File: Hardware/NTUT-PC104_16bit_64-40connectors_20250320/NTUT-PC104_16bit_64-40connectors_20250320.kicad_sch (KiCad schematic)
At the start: 15 parts, among them J14 3V3, J15 5V0, J16 GND, J17 Conn_02x26_Odd_Even, J18 Conn_02x26_Odd_Even, J19 Conn_02x26_Odd_Even, J20 Conn_02x26_Odd_Even, J21 GND, J22 GND, J23 UNREG

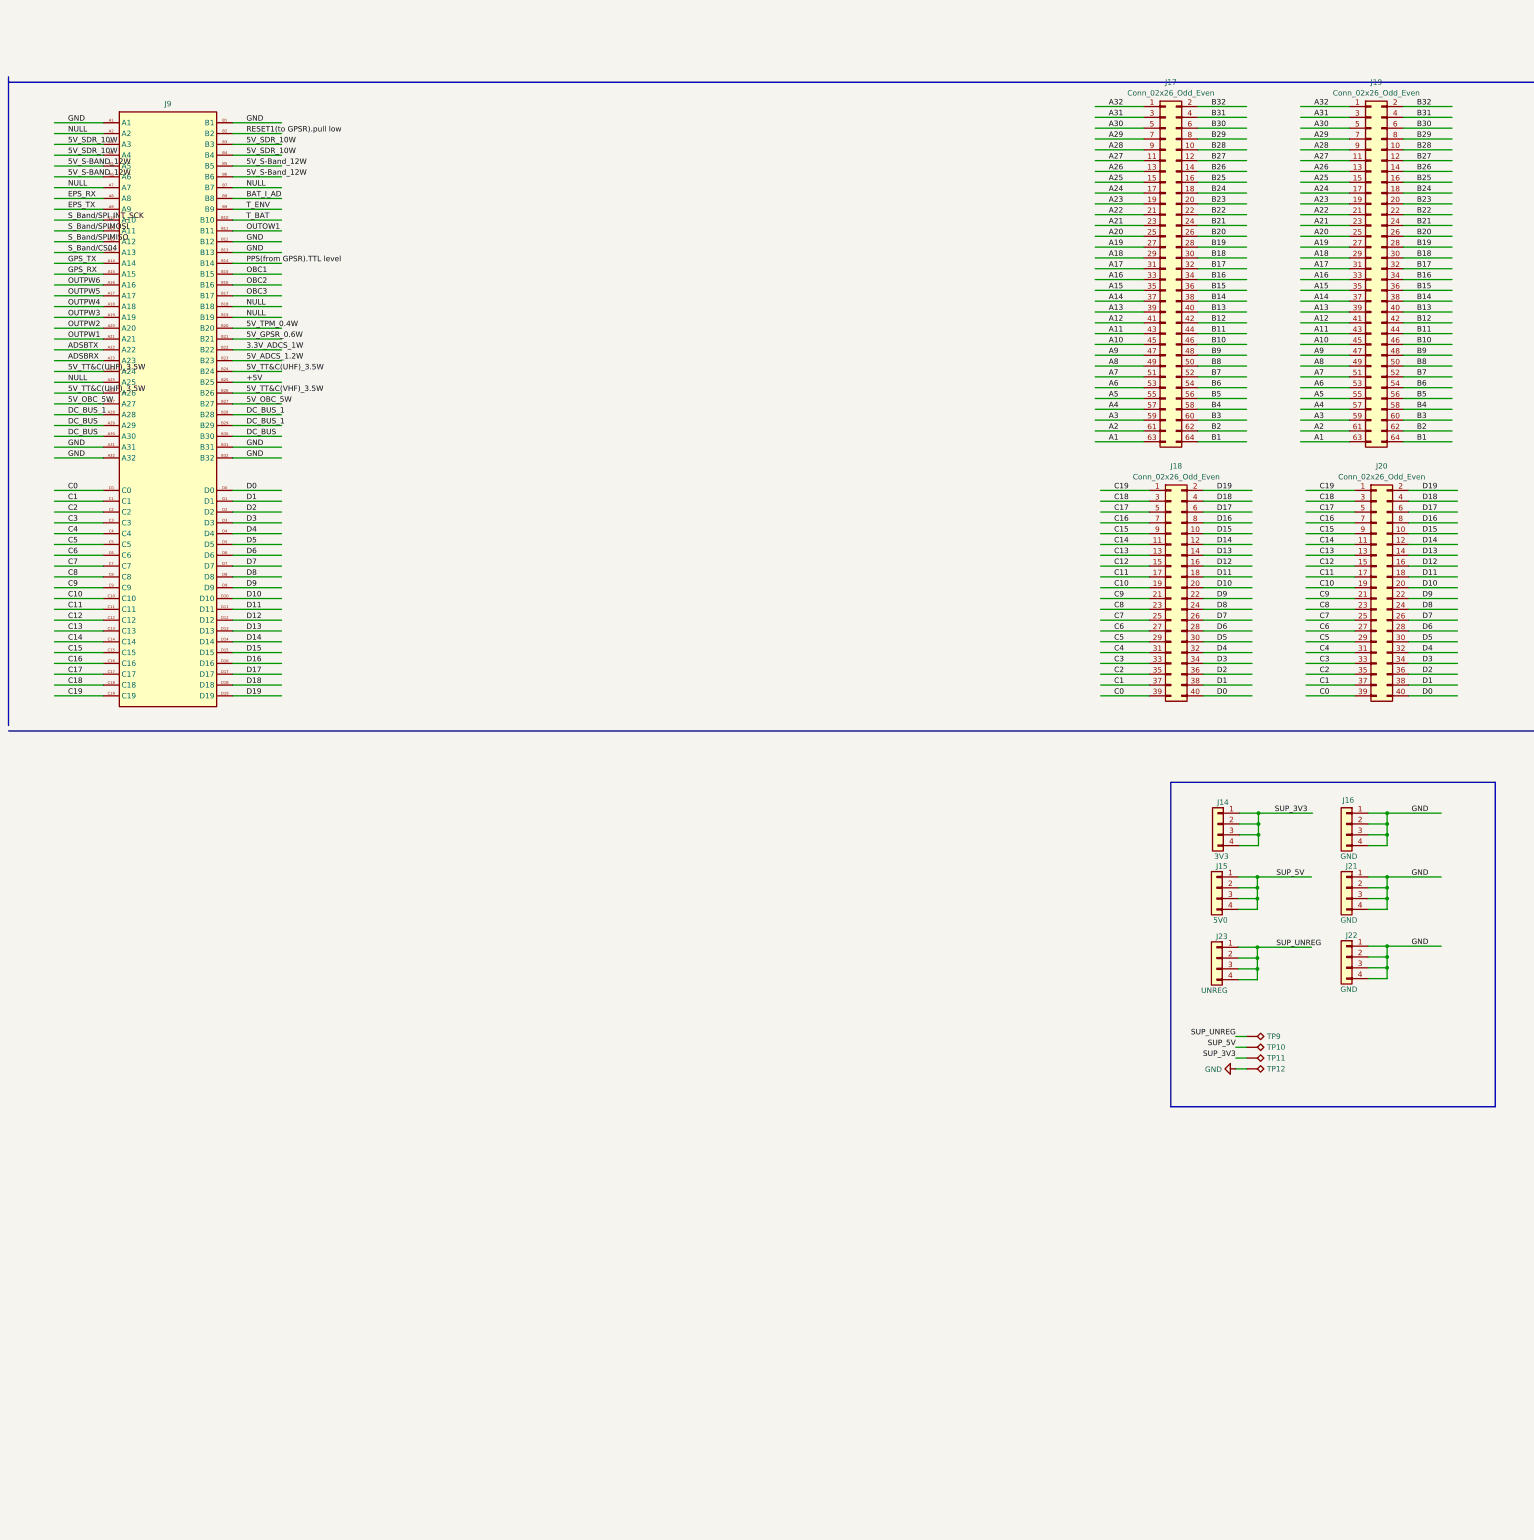
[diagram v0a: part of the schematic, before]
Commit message: Modify Schematic, assign GND to mount holes. Modify 64-pin and 40-pin labels.
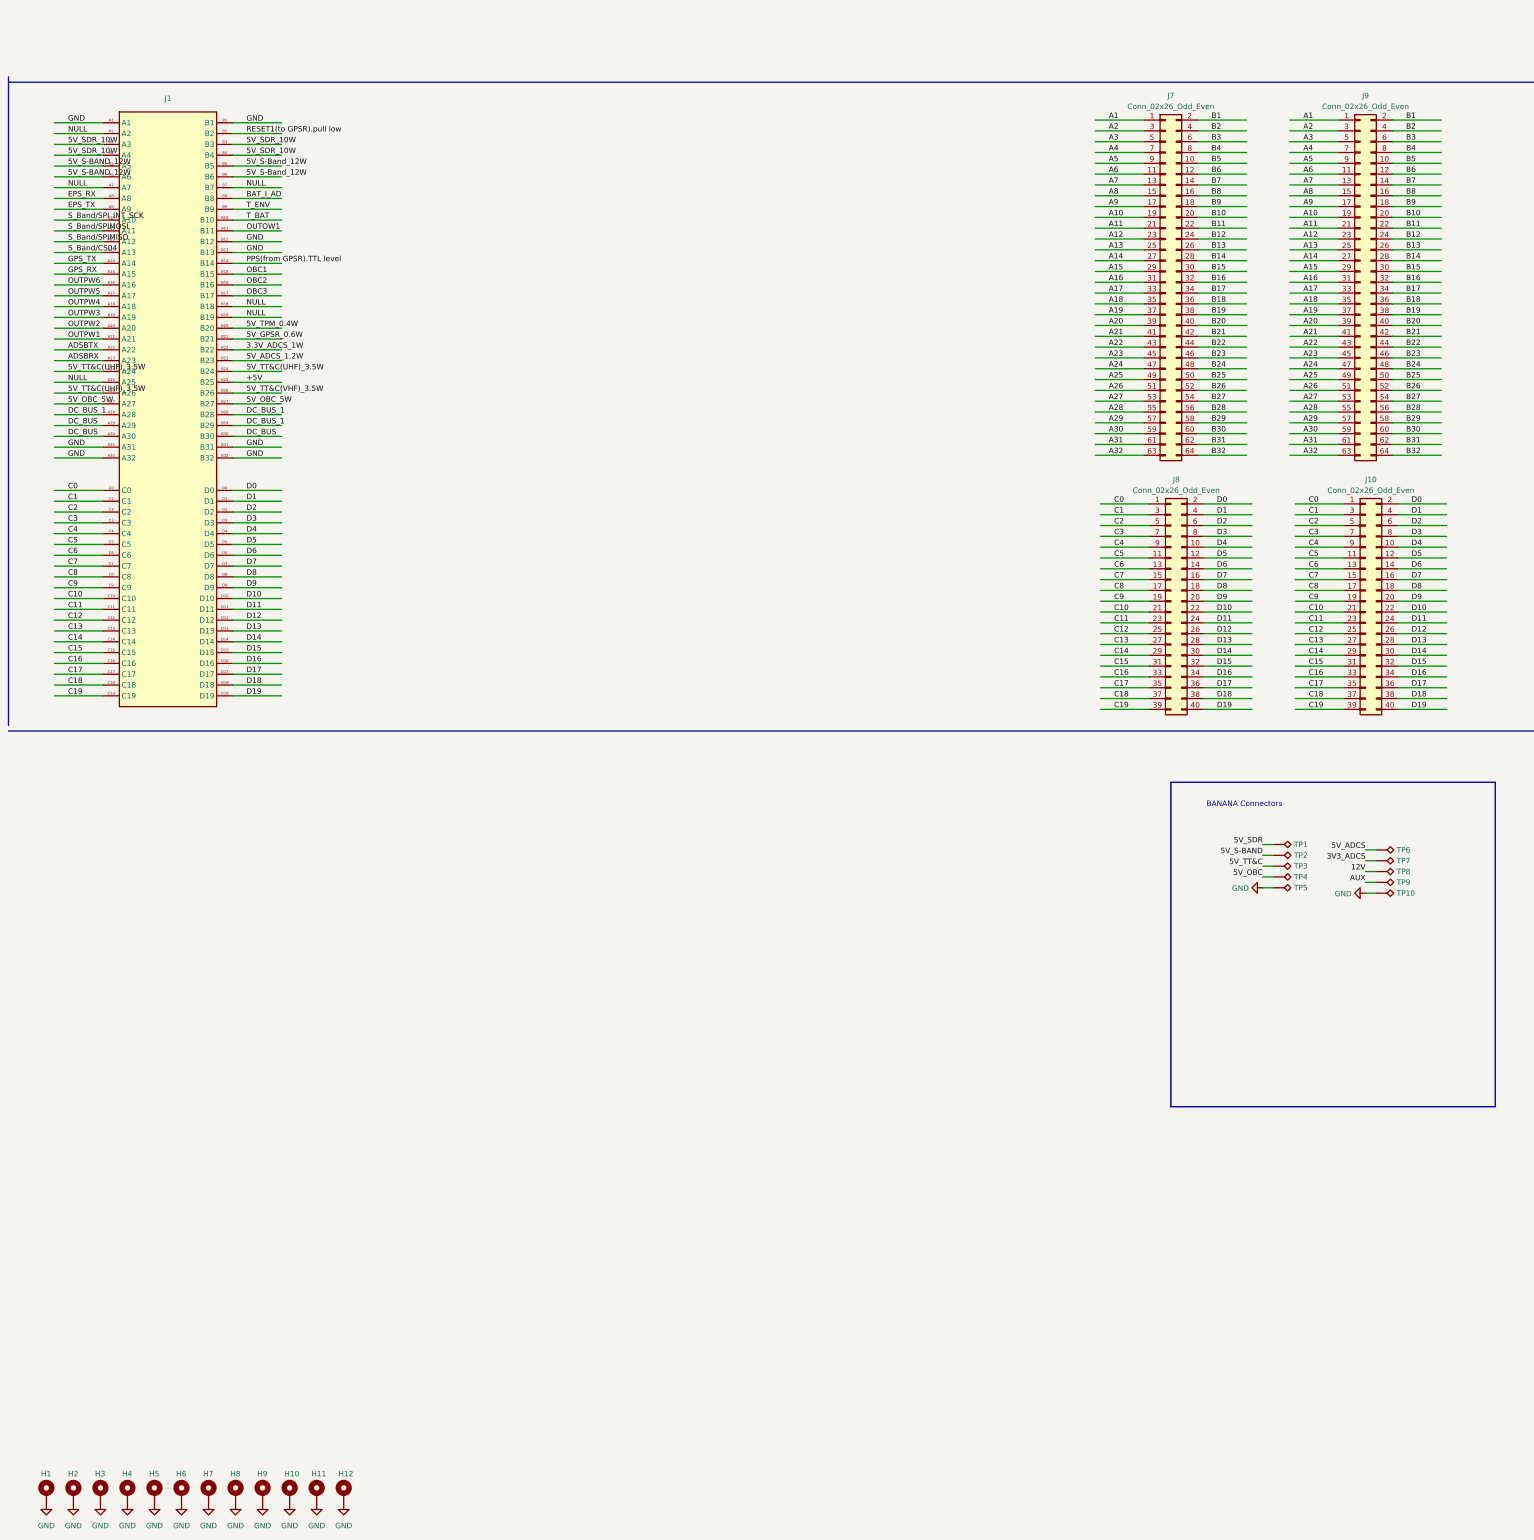
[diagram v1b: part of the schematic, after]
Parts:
- removed J14: 3V3, VST104_footprints:TSW-104-07-x-S, symbol Connector_Generic:Conn_01x04
- removed J15: 5V0, VST104_footprints:TSW-104-07-x-S, symbol Connector_Generic:Conn_01x04
- removed J16, J21, J22: GND, VST104_footprints:TSW-104-07-x-S, symbol Connector_Generic:Conn_01x04
- removed J19: Conn_02x26_Odd_Even, Connector_PinHeader_2.54mm:PinHeader_2x32_P2.54mm_Vertical, symbol Connector_Generic:Conn_02x32_Odd_Even
- removed J20: Conn_02x26_Odd_Even, Connector_PinHeader_2.54mm:PinHeader_2x20_P2.54mm_Vertical, symbol Connector_Generic:Conn_02x20_Odd_Even
- removed J23: UNREG, VST104_footprints:TSW-104-07-x-S, symbol Connector_Generic:Conn_01x04
- added H1, H10, H11, H12, H2, H3, H4, H5, H6, H7, H8, H9: MountingHole_Pad, VST104_footprints:MountingHole_3.2mm_M3_Pad_Via, symbol Mechanical:MountingHole_Pad
- added J10: Conn_02x26_Odd_Even, Connector_PinHeader_2.54mm:PinHeader_2x20_P2.54mm_Vertical, symbol Connector_Generic:Conn_02x20_Odd_Even
- added J9: Conn_02x26_Odd_Even, Connector_PinHeader_2.54mm:PinHeader_2x32_P2.54mm_Vertical, symbol Connector_Generic:Conn_02x32_Odd_Even
- added TP10, TP5, TP6, TP7, TP8, TP9: TestPoint_Alt, VST104_footprints:KSE_PN6095, symbol Connector:TestPoint_Alt
- renumbered J9 to J1, J17 to J7, J18 to J8, TP9 to TP1, TP10 to TP2, TP11 to TP3, TP12 to TP4
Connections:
- net A1: now also J7.1 (Pin_1), J9.1 (Pin_1); no longer J7.63 (Pin_63)
- net A10: now also J7.19 (Pin_19), J9.19 (Pin_19); no longer J7.45 (Pin_45)
- net A11: now also J7.21 (Pin_21), J9.21 (Pin_21); no longer J7.43 (Pin_43)
- net A12: now also J7.23 (Pin_23), J9.23 (Pin_23); no longer J7.41 (Pin_41)
- net A13: now also J7.25 (Pin_25), J9.25 (Pin_25); no longer J7.39 (Pin_39)
- net A14: now also J7.27 (Pin_27), J9.27 (Pin_27); no longer J7.37 (Pin_37)
- net A15: now also J7.29 (Pin_29), J9.29 (Pin_29); no longer J7.35 (Pin_35)
- net A16: now also J7.31 (Pin_31), J9.31 (Pin_31); no longer J7.33 (Pin_33)
- net A17: now also J7.33 (Pin_33), J9.33 (Pin_33); no longer J7.31 (Pin_31)
- net A18: now also J7.35 (Pin_35), J9.35 (Pin_35); no longer J7.29 (Pin_29)
- net A19: now also J7.37 (Pin_37), J9.37 (Pin_37); no longer J7.27 (Pin_27)
- net A2: now also J7.3 (Pin_3), J9.3 (Pin_3); no longer J7.61 (Pin_61)
- net A20: now also J7.39 (Pin_39), J9.39 (Pin_39); no longer J7.25 (Pin_25)
- net A21: now also J7.41 (Pin_41), J9.41 (Pin_41); no longer J7.23 (Pin_23)
- net A22: now also J7.43 (Pin_43), J9.43 (Pin_43); no longer J7.21 (Pin_21)
- net A23: now also J7.45 (Pin_45), J9.45 (Pin_45); no longer J7.19 (Pin_19)
- net A24: now also J7.47 (Pin_47), J9.47 (Pin_47); no longer J7.17 (Pin_17)
- net A25: now also J7.49 (Pin_49), J9.49 (Pin_49); no longer J7.15 (Pin_15)
- net A26: now also J7.51 (Pin_51), J9.51 (Pin_51); no longer J7.13 (Pin_13)
- net A27: now also J7.53 (Pin_53), J9.53 (Pin_53); no longer J7.11 (Pin_11)
- net A28: now also J7.55 (Pin_55), J9.55 (Pin_55); no longer J7.9 (Pin_9)
- net A29: now also J7.57 (Pin_57), J9.57 (Pin_57); no longer J7.7 (Pin_7)
- net A3: now also J7.5 (Pin_5), J9.5 (Pin_5); no longer J7.59 (Pin_59)
- net A30: now also J7.59 (Pin_59), J9.59 (Pin_59); no longer J7.5 (Pin_5)
- net A31: now also J7.61 (Pin_61), J9.61 (Pin_61); no longer J7.3 (Pin_3)
- net A32: now also J7.63 (Pin_63), J9.63 (Pin_63); no longer J7.1 (Pin_1)
- net A4: now also J7.7 (Pin_7), J9.7 (Pin_7); no longer J7.57 (Pin_57)
- net A5: now also J7.9 (Pin_9), J9.9 (Pin_9); no longer J7.55 (Pin_55)
- net A6: now also J7.11 (Pin_11), J9.11 (Pin_11); no longer J7.53 (Pin_53)
- net A7: now also J7.13 (Pin_13), J9.13 (Pin_13); no longer J7.51 (Pin_51)
- net A8: now also J7.15 (Pin_15), J9.15 (Pin_15); no longer J7.49 (Pin_49)
- net A9: now also J7.17 (Pin_17), J9.17 (Pin_17); no longer J7.47 (Pin_47)
- net B1: now also J7.2 (Pin_2), J9.2 (Pin_2); no longer J7.64 (Pin_64)
- net B10: now also J7.20 (Pin_20), J9.20 (Pin_20); no longer J7.46 (Pin_46)
- net B11: now also J7.22 (Pin_22), J9.22 (Pin_22); no longer J7.44 (Pin_44)
- net B12: now also J7.24 (Pin_24), J9.24 (Pin_24); no longer J7.42 (Pin_42)
- net B13: now also J7.26 (Pin_26), J9.26 (Pin_26); no longer J7.40 (Pin_40)
- net B14: now also J7.28 (Pin_28), J9.28 (Pin_28); no longer J7.38 (Pin_38)
- net B15: now also J7.30 (Pin_30), J9.30 (Pin_30); no longer J7.36 (Pin_36)
- net B16: now also J7.32 (Pin_32), J9.32 (Pin_32); no longer J7.34 (Pin_34)
- net B17: now also J7.34 (Pin_34), J9.34 (Pin_34); no longer J7.32 (Pin_32)
- net B18: now also J7.36 (Pin_36), J9.36 (Pin_36); no longer J7.30 (Pin_30)
- net B19: now also J7.38 (Pin_38), J9.38 (Pin_38); no longer J7.28 (Pin_28)
- net B2: now also J7.4 (Pin_4), J9.4 (Pin_4); no longer J7.62 (Pin_62)
- net B20: now also J7.40 (Pin_40), J9.40 (Pin_40); no longer J7.26 (Pin_26)
- net B21: now also J7.42 (Pin_42), J9.42 (Pin_42); no longer J7.24 (Pin_24)
- net B22: now also J7.44 (Pin_44), J9.44 (Pin_44); no longer J7.22 (Pin_22)
- net B23: now also J7.46 (Pin_46), J9.46 (Pin_46); no longer J7.20 (Pin_20)
- net B24: now also J7.48 (Pin_48), J9.48 (Pin_48); no longer J7.18 (Pin_18)
- net B25: now also J7.50 (Pin_50), J9.50 (Pin_50); no longer J7.16 (Pin_16)
- net B26: now also J7.52 (Pin_52), J9.52 (Pin_52); no longer J7.14 (Pin_14)
- net B27: now also J7.54 (Pin_54), J9.54 (Pin_54); no longer J7.12 (Pin_12)
- net B28: now also J7.56 (Pin_56), J9.56 (Pin_56); no longer J7.10 (Pin_10)
- net B29: now also J7.58 (Pin_58), J9.58 (Pin_58); no longer J7.8 (Pin_8)
- net B3: now also J7.6 (Pin_6), J9.6 (Pin_6); no longer J7.60 (Pin_60)
- net B30: now also J7.60 (Pin_60), J9.60 (Pin_60); no longer J7.6 (Pin_6)
- net B31: now also J7.62 (Pin_62), J9.62 (Pin_62); no longer J7.4 (Pin_4)
- net B32: now also J7.64 (Pin_64), J9.64 (Pin_64); no longer J7.2 (Pin_2)
- net B4: now also J7.8 (Pin_8), J9.8 (Pin_8); no longer J7.58 (Pin_58)
- net B5: now also J7.10 (Pin_10), J9.10 (Pin_10); no longer J7.56 (Pin_56)
- net B6: now also J7.12 (Pin_12), J9.12 (Pin_12); no longer J7.54 (Pin_54)
- net B7: now also J7.14 (Pin_14), J9.14 (Pin_14); no longer J7.52 (Pin_52)
- net B8: now also J7.16 (Pin_16), J9.16 (Pin_16); no longer J7.50 (Pin_50)
- net B9: now also J7.18 (Pin_18), J9.18 (Pin_18); no longer J7.48 (Pin_48)
- net C0: now also J8.1 (Pin_1), J10.1 (Pin_1); no longer J8.39 (Pin_39)
- net C1: now also J8.3 (Pin_3), J10.3 (Pin_3); no longer J8.37 (Pin_37)
- net C10: now also J8.21 (Pin_21), J10.21 (Pin_21); no longer J8.19 (Pin_19)
- net C11: now also J8.23 (Pin_23), J10.23 (Pin_23); no longer J8.17 (Pin_17)
- net C12: now also J8.25 (Pin_25), J10.25 (Pin_25); no longer J8.15 (Pin_15)
- net C13: now also J8.27 (Pin_27), J10.27 (Pin_27); no longer J8.13 (Pin_13)
- net C14: now also J8.29 (Pin_29), J10.29 (Pin_29); no longer J8.11 (Pin_11)
- net C15: now also J8.31 (Pin_31), J10.31 (Pin_31); no longer J8.9 (Pin_9)
- net C16: now also J8.33 (Pin_33), J10.33 (Pin_33); no longer J8.7 (Pin_7)
- net C17: now also J8.35 (Pin_35), J10.35 (Pin_35); no longer J8.5 (Pin_5)
- net C18: now also J8.37 (Pin_37), J10.37 (Pin_37); no longer J8.3 (Pin_3)
- net C19: now also J8.39 (Pin_39), J10.39 (Pin_39); no longer J8.1 (Pin_1)
- net C2: now also J8.5 (Pin_5), J10.5 (Pin_5); no longer J8.35 (Pin_35)
- net C3: now also J8.7 (Pin_7), J10.7 (Pin_7); no longer J8.33 (Pin_33)
- net C4: now also J8.9 (Pin_9), J10.9 (Pin_9); no longer J8.31 (Pin_31)
- net C5: now also J8.11 (Pin_11), J10.11 (Pin_11); no longer J8.29 (Pin_29)
- net C6: now also J8.13 (Pin_13), J10.13 (Pin_13); no longer J8.27 (Pin_27)
- net C7: now also J8.15 (Pin_15), J10.15 (Pin_15); no longer J8.25 (Pin_25)
- net C8: now also J8.17 (Pin_17), J10.17 (Pin_17); no longer J8.23 (Pin_23)
- net C9: now also J8.19 (Pin_19), J10.19 (Pin_19); no longer J8.21 (Pin_21)
- net D0: now also J8.2 (Pin_2), J10.2 (Pin_2); no longer J8.40 (Pin_40)
- net D1: now also J8.4 (Pin_4), J10.4 (Pin_4); no longer J8.38 (Pin_38)
- net D10: now also J8.22 (Pin_22), J10.22 (Pin_22); no longer J8.20 (Pin_20)
- net D11: now also J8.24 (Pin_24), J10.24 (Pin_24); no longer J8.18 (Pin_18)
- net D12: now also J8.26 (Pin_26), J10.26 (Pin_26); no longer J8.16 (Pin_16)
- net D13: now also J8.28 (Pin_28), J10.28 (Pin_28); no longer J8.14 (Pin_14)
- net D14: now also J8.30 (Pin_30), J10.30 (Pin_30); no longer J8.12 (Pin_12)
- net D15: now also J8.32 (Pin_32), J10.32 (Pin_32); no longer J8.10 (Pin_10)
- net D16: now also J8.34 (Pin_34), J10.34 (Pin_34); no longer J8.8 (Pin_8)
- net D17: now also J8.36 (Pin_36), J10.36 (Pin_36); no longer J8.6 (Pin_6)
- net D18: now also J8.38 (Pin_38), J10.38 (Pin_38); no longer J8.4 (Pin_4)
- net D19: now also J8.40 (Pin_40), J10.40 (Pin_40); no longer J8.2 (Pin_2)
- net D2: now also J8.6 (Pin_6), J10.6 (Pin_6); no longer J8.36 (Pin_36)
- net D3: now also J8.8 (Pin_8), J10.8 (Pin_8); no longer J8.34 (Pin_34)
- net D4: now also J8.10 (Pin_10), J10.10 (Pin_10); no longer J8.32 (Pin_32)
- net D5: now also J8.12 (Pin_12), J10.12 (Pin_12); no longer J8.30 (Pin_30)
- net D6: now also J8.14 (Pin_14), J10.14 (Pin_14); no longer J8.28 (Pin_28)
- net D7: now also J8.16 (Pin_16), J10.16 (Pin_16); no longer J8.26 (Pin_26)
- net D8: now also J8.18 (Pin_18), J10.18 (Pin_18); no longer J8.24 (Pin_24)
- net D9: now also J8.20 (Pin_20), J10.20 (Pin_20); no longer J8.22 (Pin_22)
- net GND: now also H1.1, H10.1, H11.1, H12.1, H2.1, H3.1, H4.1, H5.1, H6.1, H7.1, H8.1, H9.1, TP10.1, TP5.1; no longer TP4.1
- net SUP_3V3 renamed 5V_TT&C
- net SUP_5V renamed 5V_S-BAND
- net SUP_UNREG renamed 5V_SDR
- new net 12V: TP8.1
- new net 3V3_ADCS: TP7.1
- new net 5V_ADCS: TP6.1
- new net 5V_OBC: TP4.1
- new net AUX: TP9.1
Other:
- note added: "BANANA Connectors"
- moved on the sheet: J7, J8, TP1, TP2, TP3, TP4

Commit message: 1. Add all six boards. 2. Assign Parus pins to every board. 3. Change foot-print path to project directory such that the project    will not rely on external footprints. 4. Copy 'CubeSat_PC104_16bit_footprint.kicad_mod',    'CubeSat_PC104_16bit_footprint_15mm.kicad_mod' and    'CubeSat_PC104_16bit_footprint_Edge.Cut.kicad_mod' to project footprint    directory. 5. Add connectors between banana connectors and all other boards.
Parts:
- added J11: ~, VST104_footprints:PC104_16bit_Connector, symbol VST104_symbols:PC104
- added J12, J13, J14, J15, J16, J17, J18, J7: Conn_02x04_Odd_Even, Connector_PinHeader_2.54mm:PinHeader_2x04_P2.54mm_Vertical, symbol Connector_Generic:Conn_02x04_Odd_Even
- added J2, J3, J4, J5, J6: ~, VST104_footprints:CubeSat_PC104_16bit_footprint, symbol VST104_symbols:PC104
- renumbered J7 to JA19
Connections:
- net A1 is gone; now on net GND: J9.1 (Pin_1), JA19.1 (Pin_1)
- net A10 is gone; now on net S_Band/SPI_INT_SCK: J9.19 (Pin_19), JA19.19 (Pin_19)
- net A11 is gone; now on net S_Band/SPIMOSI: J9.21 (Pin_21), JA19.21 (Pin_21)
- net A12 is gone; now on net S_Band/SPIMISO: J9.23 (Pin_23), JA19.23 (Pin_23)
- net A13 is gone; now on net S_Band/CS04: J9.25 (Pin_25), JA19.25 (Pin_25)
- net A14 is gone; now on net GPS_TX: J9.27 (Pin_27), JA19.27 (Pin_27)
- net A15 is gone; now on net GPS_RX: J9.29 (Pin_29), JA19.29 (Pin_29)
- net A16 is gone; now on net OUTPW6: J9.31 (Pin_31), JA19.31 (Pin_31)
- net A17 is gone; now on net OUTPW5: J9.33 (Pin_33), JA19.33 (Pin_33)
- net A18 is gone; now on net OUTPW4: J9.35 (Pin_35), JA19.35 (Pin_35)
- net A19 is gone; now on net OUTPW3: J9.37 (Pin_37), JA19.37 (Pin_37)
- net A20 is gone; now on net OUTPW2: J9.39 (Pin_39), JA19.39 (Pin_39)
- net A21 is gone; now on net OUTPW1: J9.41 (Pin_41), JA19.41 (Pin_41)
- net A22 is gone; now on net ADSBTX: J9.43 (Pin_43), JA19.43 (Pin_43)
- net A23 is gone; now on net ADSBRX: J9.45 (Pin_45), JA19.45 (Pin_45)
- net A24 is gone; now on net 5V_TT&C(UHF)_3.5W: J9.47 (Pin_47), JA19.47 (Pin_47)
- net A26 is gone; now on net 5V_TT&C(VHF)_3.5W: J9.51 (Pin_51), JA19.51 (Pin_51)
- net A27 is gone; now on net 5V_OBC_5W: J9.53 (Pin_53), JA19.53 (Pin_53)
- net A28 is gone; now on net DC_BUS_1: J9.55 (Pin_55), JA19.55 (Pin_55)
- net A29 is gone; now on net DC_BUS: J9.57 (Pin_57), JA19.57 (Pin_57)
- net A3 is gone; now on net 5V_SDR_10W: J9.5 (Pin_5), JA19.5 (Pin_5)
- net A30 is gone; now on net DC_BUS: J9.59 (Pin_59), JA19.59 (Pin_59)
- net A31 is gone; now on net GND: J9.61 (Pin_61), JA19.61 (Pin_61)
- net A32 is gone; now on net GND: J9.63 (Pin_63), JA19.63 (Pin_63)
- net A4 is gone; now on net 5V_SDR_10W: J9.7 (Pin_7), JA19.7 (Pin_7)
- net A5 is gone; now on net 5V_S-BAND_12W: J9.9 (Pin_9), JA19.9 (Pin_9)
- net A6 is gone; now on net 5V_S-BAND_12W: J9.11 (Pin_11), JA19.11 (Pin_11)
- net A8 is gone; now on net EPS_RX: J9.15 (Pin_15), JA19.15 (Pin_15)
- net A9 is gone; now on net EPS_TX: J9.17 (Pin_17), JA19.17 (Pin_17)
- net B1 is gone; now on net GND: J9.2 (Pin_2), JA19.2 (Pin_2)
- net B10 is gone; now on net T_BAT: J9.20 (Pin_20), JA19.20 (Pin_20)
- net B11 is gone; now on net OUTOW1: J9.22 (Pin_22), JA19.22 (Pin_22)
- net B12 is gone; now on net GND: J9.24 (Pin_24), JA19.24 (Pin_24)
- net B13 is gone; now on net GND: J9.26 (Pin_26), JA19.26 (Pin_26)
- net B15 is gone; now on net OBC1: J9.30 (Pin_30), JA19.30 (Pin_30)
- net B16 is gone; now on net OBC2: J9.32 (Pin_32), JA19.32 (Pin_32)
- net B17 is gone; now on net OBC3: J9.34 (Pin_34), JA19.34 (Pin_34)
- net B20 is gone; now on net 5V_TPM_0.4W: J9.40 (Pin_40), JA19.40 (Pin_40)
- net B21 is gone; now on net 5V_GPSR_0.6W: J9.42 (Pin_42), JA19.42 (Pin_42)
- net B22 is gone; now on net 3.3V_ADCS_1W: J9.44 (Pin_44), JA19.44 (Pin_44)
- net B23 is gone; now on net 5V_ADCS_1.2W: J9.46 (Pin_46), JA19.46 (Pin_46)
- net B24 is gone; now on net 5V_TT&C(UHF)_3.5W: J9.48 (Pin_48), JA19.48 (Pin_48)
- net B25 is gone; now on net +5V: J9.50 (Pin_50), JA19.50 (Pin_50)
- net B26 is gone; now on net 5V_TT&C(VHF)_3.5W: J9.52 (Pin_52), JA19.52 (Pin_52)
- net B27 is gone; now on net 5V_OBC_5W: J9.54 (Pin_54), JA19.54 (Pin_54)
- net B28 is gone; now on net DC_BUS_1: J9.56 (Pin_56), JA19.56 (Pin_56)
- net B29 is gone; now on net DC_BUS_1: J9.58 (Pin_58), JA19.58 (Pin_58)
- net B3 is gone; now on net 5V_SDR_10W: J9.6 (Pin_6), JA19.6 (Pin_6)
- net B30 is gone; now on net DC_BUS: J9.60 (Pin_60), JA19.60 (Pin_60)
- net B31 is gone; now on net GND: J9.62 (Pin_62), JA19.62 (Pin_62)
- net B32 is gone; now on net GND: J9.64 (Pin_64), JA19.64 (Pin_64)
- net B4 is gone; now on net 5V_SDR_10W: J9.8 (Pin_8), JA19.8 (Pin_8)
- net B5 is gone; now on net 5V_S-Band_12W: J9.10 (Pin_10), JA19.10 (Pin_10)
- net B6 is gone; now on net 5V_S-Band_12W: J9.12 (Pin_12), JA19.12 (Pin_12)
- net B8 is gone; now on net BAT_I_AD: J9.16 (Pin_16), JA19.16 (Pin_16)
- net B9 is gone; now on net T_ENV: J9.18 (Pin_18), JA19.18 (Pin_18)
- net PPS(from GPSR).TTL level is gone; now on net PPS: J1.B14
- net RESET1(to GPSR).pull low is gone; now on net RESET1: J1.B2
- net +5V: now also J11.B25, J2.B25, J3.B25, J4.B25, J5.B25, J6.B25
- net 12V: now also J17.1 (Pin_1), J17.3 (Pin_3), J17.5 (Pin_5), J17.7 (Pin_7)
- net 3.3V_ADCS_1W: now also J11.B22, J16.2 (Pin_2), J16.4 (Pin_4), J16.6 (Pin_6), J16.8 (Pin_8), J2.B22, J3.B22, J4.B22, J5.B22, J6.B22
- net 3V3_ADCS: now also J16.1 (Pin_1), J16.3 (Pin_3), J16.5 (Pin_5), J16.7 (Pin_7)
- net 5V_ADCS: now also J15.1 (Pin_1), J15.3 (Pin_3), J15.5 (Pin_5), J15.7 (Pin_7)
- net 5V_ADCS_1.2W: now also J11.B23, J15.2 (Pin_2), J15.4 (Pin_4), J15.6 (Pin_6), J15.8 (Pin_8), J2.B23, J3.B23, J4.B23, J5.B23, J6.B23
- net 5V_GPSR_0.6W: now also J11.B21, J18.6 (Pin_6), J18.8 (Pin_8), J2.B21, J3.B21, J4.B21, J5.B21, J6.B21
- net 5V_OBC: now also J14.1 (Pin_1), J14.3 (Pin_3), J14.5 (Pin_5), J14.7 (Pin_7)
- net 5V_OBC_5W: now also J11.A27, J11.B27, J14.2 (Pin_2), J14.4 (Pin_4), J14.6 (Pin_6), J14.8 (Pin_8), J2.A27, J2.B27, J3.A27, J3.B27, J4.A27, J4.B27, J5.A27, J5.B27, J6.A27, J6.B27
- net 5V_S-BAND: now also J12.1 (Pin_1), J12.3 (Pin_3), J12.5 (Pin_5), J12.7 (Pin_7)
- net 5V_S-BAND_12W: now also J11.A5, J11.A6, J12.2 (Pin_2), J12.4 (Pin_4), J12.6 (Pin_6), J12.8 (Pin_8), J2.A5, J2.A6, J3.A5, J3.A6, J4.A5, J4.A6, J5.A5, J5.A6, J6.A5, J6.A6
- net 5V_S-Band_12W: now also J11.B5, J11.B6, J2.B5, J2.B6, J3.B5, J3.B6, J4.B5, J4.B6, J5.B5, J5.B6, J6.B5, J6.B6
- net 5V_SDR: now also J7.1 (Pin_1), J7.3 (Pin_3), J7.5 (Pin_5), J7.7 (Pin_7)
- net 5V_SDR_10W: now also J11.A3, J11.A4, J11.B3, J11.B4, J2.A3, J2.A4, J2.B3, J2.B4, J3.A3, J3.A4, J3.B3, J3.B4, J4.A3, J4.A4, J4.B3, J4.B4, J5.A3, J5.A4, J5.B3, J5.B4, J6.A3, J6.A4, J6.B3, J6.B4, J7.2 (Pin_2), J7.4 (Pin_4), J7.6 (Pin_6), J7.8 (Pin_8)
- net 5V_TPM_0.4W: now also J11.B20, J18.2 (Pin_2), J18.4 (Pin_4), J2.B20, J3.B20, J4.B20, J5.B20, J6.B20
- net 5V_TT&C: now also J13.1 (Pin_1), J13.3 (Pin_3), J13.5 (Pin_5), J13.7 (Pin_7)
- net 5V_TT&C(UHF)_3.5W: now also J11.A24, J11.B24, J13.6 (Pin_6), J13.8 (Pin_8), J2.A24, J2.B24, J3.A24, J3.B24, J4.A24, J4.B24, J5.A24, J5.B24, J6.A24, J6.B24; no longer J1.A26
- net 5V_TT&C(VHF)_3.5W: now also J1.A26, J11.A26, J11.B26, J13.2 (Pin_2), J13.4 (Pin_4), J2.A26, J2.B26, J3.A26, J3.B26, J4.A26, J4.B26, J5.A26, J5.B26, J6.A26, J6.B26
- net ADSBRX: now also J11.A23, J2.A23, J3.A23, J4.A23, J5.A23, J6.A23
- net ADSBTX: now also J11.A22, J2.A22, J3.A22, J4.A22, J5.A22, J6.A22
- net BAT_I_AD: now also J11.B8, J2.B8, J3.B8, J4.B8, J5.B8, J6.B8
- net C0: now also J11.C0, J2.C0, J3.C0, J4.C0, J5.C0, J6.C0
- net C1: now also J11.C1, J2.C1, J3.C1, J4.C1, J5.C1, J6.C1
- net C10: now also J11.C10, J2.C10, J3.C10, J4.C10, J5.C10, J6.C10
- net C11: now also J11.C11, J2.C11, J3.C11, J4.C11, J5.C11, J6.C11
- net C12: now also J11.C12, J2.C12, J3.C12, J4.C12, J5.C12, J6.C12
- net C13: now also J11.C13, J2.C13, J3.C13, J4.C13, J5.C13, J6.C13
- net C14: now also J11.C14, J2.C14, J3.C14, J4.C14, J5.C14, J6.C14
- net C15: now also J11.C15, J2.C15, J3.C15, J4.C15, J5.C15, J6.C15
- net C16: now also J11.C16, J2.C16, J3.C16, J4.C16, J5.C16, J6.C16
- net C17: now also J11.C17, J2.C17, J3.C17, J4.C17, J5.C17, J6.C17
- net C18: now also J11.C18, J2.C18, J3.C18, J4.C18, J5.C18, J6.C18
- net C19: now also J11.C19, J2.C19, J3.C19, J4.C19, J5.C19, J6.C19
- net C2: now also J11.C2, J2.C2, J3.C2, J4.C2, J5.C2, J6.C2
- net C3: now also J11.C3, J2.C3, J3.C3, J4.C3, J5.C3, J6.C3
- net C4: now also J11.C4, J2.C4, J3.C4, J4.C4, J5.C4, J6.C4
- net C5: now also J11.C5, J2.C5, J3.C5, J4.C5, J5.C5, J6.C5
- net C6: now also J11.C6, J2.C6, J3.C6, J4.C6, J5.C6, J6.C6
- net C7: now also J11.C7, J2.C7, J3.C7, J4.C7, J5.C7, J6.C7
- net C8: now also J11.C8, J2.C8, J3.C8, J4.C8, J5.C8, J6.C8
- net C9: now also J11.C9, J2.C9, J3.C9, J4.C9, J5.C9, J6.C9
- net D0: now also J11.D0, J2.D0, J3.D0, J4.D0, J5.D0, J6.D0
- net D1: now also J11.D1, J2.D1, J3.D1, J4.D1, J5.D1, J6.D1
- net D10: now also J11.D10, J2.D10, J3.D10, J4.D10, J5.D10, J6.D10
- net D11: now also J11.D11, J2.D11, J3.D11, J4.D11, J5.D11, J6.D11
- net D12: now also J11.D12, J2.D12, J3.D12, J4.D12, J5.D12, J6.D12
- net D13: now also J11.D13, J2.D13, J3.D13, J4.D13, J5.D13, J6.D13
- net D14: now also J11.D14, J2.D14, J3.D14, J4.D14, J5.D14, J6.D14
- net D15: now also J11.D15, J2.D15, J3.D15, J4.D15, J5.D15, J6.D15
- net D16: now also J11.D16, J2.D16, J3.D16, J4.D16, J5.D16, J6.D16
- net D17: now also J11.D17, J2.D17, J3.D17, J4.D17, J5.D17, J6.D17
- net D18: now also J11.D18, J2.D18, J3.D18, J4.D18, J5.D18, J6.D18
- net D19: now also J11.D19, J2.D19, J3.D19, J4.D19, J5.D19, J6.D19
- net D2: now also J11.D2, J2.D2, J3.D2, J4.D2, J5.D2, J6.D2
- net D3: now also J11.D3, J2.D3, J3.D3, J4.D3, J5.D3, J6.D3
- net D4: now also J11.D4, J2.D4, J3.D4, J4.D4, J5.D4, J6.D4
- net D5: now also J11.D5, J2.D5, J3.D5, J4.D5, J5.D5, J6.D5
- net D6: now also J11.D6, J2.D6, J3.D6, J4.D6, J5.D6, J6.D6
- net D7: now also J11.D7, J2.D7, J3.D7, J4.D7, J5.D7, J6.D7
- net D8: now also J11.D8, J2.D8, J3.D8, J4.D8, J5.D8, J6.D8
- net D9: now also J11.D9, J2.D9, J3.D9, J4.D9, J5.D9, J6.D9
- net DC_BUS: now also J11.A29, J11.A30, J11.B30, J2.A29, J2.A30, J2.B30, J3.A29, J3.A30, J3.B30, J4.A29, J4.A30, J4.B30, J5.A29, J5.A30, J5.B30, J6.A29, J6.A30, J6.B30
- net DC_BUS_1: now also J11.A28, J11.B28, J11.B29, J2.A28, J2.B28, J2.B29, J3.A28, J3.B28, J3.B29, J4.A28, J4.B28, J4.B29, J5.A28, J5.B28, J5.B29, J6.A28, J6.B28, J6.B29
- net EPS_RX: now also J11.A8, J2.A8, J3.A8, J4.A8, J5.A8, J6.A8
- net EPS_TX: now also J11.A9, J2.A9, J3.A9, J4.A9, J5.A9, J6.A9
- net GND: now also J11.A1, J11.A31, J11.A32, J11.B1, J11.B12, J11.B13, J11.B31, J11.B32, J2.A1, J2.A31, J2.A32, J2.B1, J2.B12, J2.B13, J2.B31, J2.B32, J3.A1, J3.A31, J3.A32, J3.B1, J3.B12, J3.B13, J3.B31, J3.B32, J4.A1, J4.A31, J4.A32, J4.B1, J4.B12, J4.B13, J4.B31, J4.B32, J5.A1, J5.A31, J5.A32, J5.B1, J5.B12, J5.B13, J5.B31, J5.B32, J6.A1, J6.A31, J6.A32, J6.B1, J6.B12, J6.B13, J6.B31, J6.B32
- net GPS_RX: now also J11.A15, J2.A15, J3.A15, J4.A15, J5.A15, J6.A15
- net GPS_TX: now also J11.A14, J2.A14, J3.A14, J4.A14, J5.A14, J6.A14
- net OBC1: now also J11.B15, J2.B15, J3.B15, J4.B15, J5.B15, J6.B15
- net OBC2: now also J11.B16, J2.B16, J3.B16, J4.B16, J5.B16, J6.B16
- net OBC3: now also J11.B17, J2.B17, J3.B17, J4.B17, J5.B17, J6.B17
- net OUTOW1: now also J11.B11, J2.B11, J3.B11, J4.B11, J5.B11, J6.B11
- net OUTPW1: now also J11.A21, J2.A21, J3.A21, J4.A21, J5.A21, J6.A21
- net OUTPW2: now also J11.A20, J2.A20, J3.A20, J4.A20, J5.A20, J6.A20
- net OUTPW3: now also J11.A19, J2.A19, J3.A19, J4.A19, J5.A19, J6.A19
- net OUTPW4: now also J11.A18, J2.A18, J3.A18, J4.A18, J5.A18, J6.A18
- net OUTPW5: now also J11.A17, J2.A17, J3.A17, J4.A17, J5.A17, J6.A17
- net OUTPW6: now also J11.A16, J2.A16, J3.A16, J4.A16, J5.A16, J6.A16
- net S_Band/CS04: now also J11.A13, J2.A13, J3.A13, J4.A13, J5.A13, J6.A13
- net S_Band/SPIMISO: now also J11.A12, J2.A12, J3.A12, J4.A12, J5.A12, J6.A12
- net S_Band/SPIMOSI: now also J11.A11, J2.A11, J3.A11, J4.A11, J5.A11, J6.A11
- net S_Band/SPI_INT_SCK: now also J11.A10, J2.A10, J3.A10, J4.A10, J5.A10, J6.A10
- net T_BAT: now also J11.B10, J2.B10, J3.B10, J4.B10, J5.B10, J6.B10
- net T_ENV: now also J11.B9, J2.B9, J3.B9, J4.B9, J5.B9, J6.B9
- net A2 renamed NULL1
- net NULL1: now also J1.A2, J11.A2, J2.A2, J3.A2, J4.A2, J5.A2, J6.A2
- net A25 renamed NULL3
- net NULL3: now also J1.A25, J11.A25, J2.A25, J3.A25, J4.A25, J5.A25, J6.A25
- net A7 renamed NULL2
- net NULL2: now also J1.A7, J11.A7, J2.A7, J3.A7, J4.A7, J5.A7, J6.A7
- net AUX renamed 5V
- net 5V: now also J18.1 (Pin_1), J18.3 (Pin_3), J18.5 (Pin_5), J18.7 (Pin_7)
- net B14 renamed PPS
- net PPS: now also J11.B14, J2.B14, J3.B14, J4.B14, J5.B14, J6.B14
- net B18 renamed NULL5
- net NULL5: now also J1.B18, J11.B18, J2.B18, J3.B18, J4.B18, J5.B18, J6.B18
- net B19 renamed NULL6
- net NULL6: now also J1.B19, J11.B19, J2.B19, J3.B19, J4.B19, J5.B19, J6.B19
- net B2 renamed RESET1
- net RESET1: now also J11.B2, J2.B2, J3.B2, J4.B2, J5.B2, J6.B2
- net B7 renamed NULL4
- net NULL4: now also J1.B7, J11.B7, J2.B7, J3.B7, J4.B7, J5.B7, J6.B7
- removed net NULL: J1.A2, J1.A25, J1.A7, J1.B18, J1.B19, J1.B7
- new net: J17.2 (Pin_2), J17.4 (Pin_4), J17.6 (Pin_6), J17.8 (Pin_8)
- no-connect marks 1 -> 2
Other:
- note added: "A1"
- note added: "A10"
- note added: "A11"
- note added: "A12"
- note added: "A13"
- note added: "A14"
- note added: "A15"
- note added: "A16"
- note added: "A17"
- note added: "A18"
- note added: "A19"
- note added: "A2"
- note added: "A20"
- note added: "A21"
- note added: "A22"
- note added: "A23"
- note added: "A24"
- note added: "A25"
- note added: "A26"
- note added: "A27"
- note added: "A28"
- note added: "A29"
- note added: "A3"
- note added: "A30"
- note added: "A31"
- note added: "A32"
- note added: "A4"
- note added: "A5"
- note added: "A6"
- note added: "A7"
- note added: "A8"
- note added: "A9"
- note added: "B1"
- note added: "B10"
- note added: "B11"
- note added: "B12"
- note added: "B13"
- note added: "B14"
- note added: "B15"
- note added: "B16"
- note added: "B17"
- note added: "B18"
- note added: "B19"
- note added: "B2"
- note added: "B20"
- note added: "B21"
- note added: "B22"
- note added: "B23"
- note added: "B24"
- note added: "B25"
- note added: "B26"
- note added: "B27"
- note added: "B28"
- note added: "B29"
- note added: "B3"
- note added: "B30"
- note added: "B31"
- note added: "B32"
- note added: "B4"
- note added: "B5"
- note added: "B6"
- note added: "B7"
- note added: "B8"
- note added: "B9"
- note added: "C0"
- note added: "C1"
- note added: "C10"
- note added: "C11"
- note added: "C12"
- note added: "C13"
- note added: "C14"
- note added: "C15"
- note added: "C16"
- note added: "C17"
- note added: "C18"
- note added: "C19"
- note added: "C2"
- note added: "C3"
- note added: "C4"
- note added: "C5"
- note added: "C6"
- note added: "C7"
- note added: "C8"
- note added: "C9"
- note added: "D0"
- note added: "D1"
- note added: "D10"
- note added: "D11"
- note added: "D12"
- note added: "D13"
- note added: "D14"
- note added: "D15"
- note added: "D16"
- note added: "D17"
- note added: "D18"
- note added: "D19"
- note added: "D2"
- note added: "D3"
- note added: "D4"
- note added: "D5"
- note added: "D6"
- note added: "D8"
- note added: "D9"
- note added: "Extension Connectors"
- note added: "Extension PC104 Connectors"
- note added: "Mount Holes"
- note added: "PC104 Boards"
- company: VisionSpace Technologies -> NTUT/TASA
- title: VST104 flat-sat -> Parus flat-sat
- moved on the sheet: H1, H10, H11, H12, H2, H3, H4, H5, H6, H7, H8, H9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
